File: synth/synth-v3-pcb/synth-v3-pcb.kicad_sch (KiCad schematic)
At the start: 34 parts, among them J1 Keyboard, J2 15mm Touch, J3 15mm Touch, U4 Pi Pico, U5 TC1044S

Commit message: Released Synth V3.0
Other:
- company: (none) -> LiveWires
- title: (none) -> LW Synth
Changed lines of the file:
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@@
 	(generator_version "9.0")
 	(paper "A4")
+	(title_block
+		(title "LW Synth")
+		(date "2026-01-06")
+		(rev "3.0")
+		(company "LiveWires")
+	)
 	(text "Power Regulator"
 		(exclude_from_sim no)
@@
 		)
 		(instances
-			(project "synth-v1"
+			(project "synth-v3-pcb"
 				(path "/e4b14e5f-7937-4e93-a8ca-bc52b5b8338f"
 					(page "2")

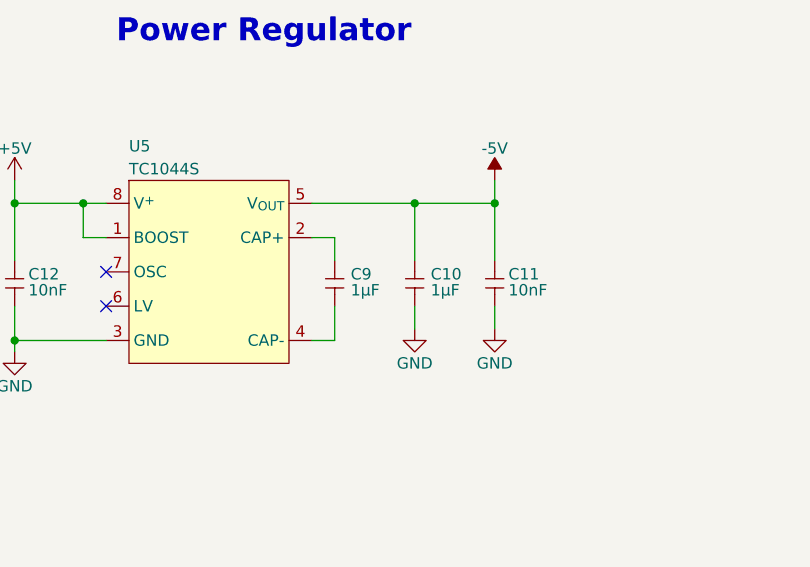
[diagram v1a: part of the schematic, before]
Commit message: Released PCB v3.1 and added knobs
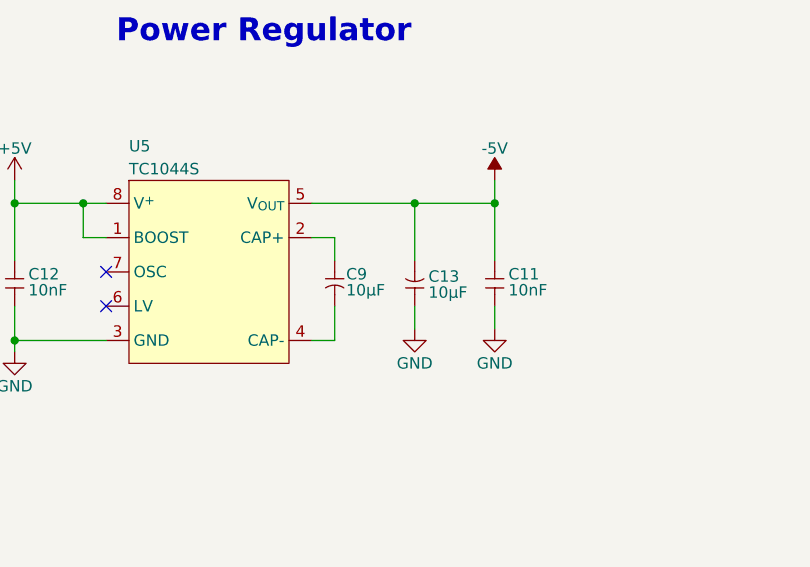
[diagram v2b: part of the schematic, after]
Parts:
- removed C10, C9: 1µF, LiveWires:LW_CeramicCap_5.08mm, symbol LiveWires:LW_C-1u
- added C13, C9: 10µF, LiveWires:LW_CAP_Radial_D5.0mm_P2.00mm, symbol LiveWires:LW_C-10u
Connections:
- net -5V: now also C13.2
- net GND: now also C13.1
- net at U5.2 (CAP+): now also C9.1
- net at U5.4 (CAP-): now also C9.2
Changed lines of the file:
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@@
-	)
-	(symbol
-		(lib_id "LiveWires:LW_C-1u")
-		(at 102.87 162.56 90)
-		(unit 1)
-		(exclude_from_sim no)
-		(in_bom yes)
-		(on_board yes)
-		(dnp no)
-		(property "Reference" "C10"
-			(at 104.648 161.544 90)
-			(effects
-				(font
-					(size 1.27 1.27)
-				)
-				(justify right)
-			)
-		)
-		(property "Value" "1µF"
-			(at 104.648 163.322 90)
-			(effects
-				(font
-					(size 1.27 1.27)
-				)
-				(justify right)
-			)
-		)
-		(property "Footprint" "LiveWires:LW_CeramicCap_5.08mm"
-			(at 102.87 162.56 0)
-			(effects
-				(font
-					(size 1.27 1.27)
-				)
-				(hide yes)
-			)
-		)
-		(property "Datasheet" ""
-			(at 102.87 162.56 0)
-			(effects
-				(font
-					(size 1.27 1.27)
-				)
-				(hide yes)
-			)
-		)
-		(property "Description" "1µF Ceramic Capacitor (generic)"
-			(at 102.87 162.56 0)
-			(effects
-				(font
-					(size 1.27 1.27)
-				)
-				(hide yes)
-			)
-		)
-		(property "Cost" "0.07"
-			(at 102.87 162.56 0)
-			(effects
-				(font
-					(size 1.27 1.27)
-				)
-				(hide yes)
-			)
-		)
-		(property "MPN" "TS170R1H105MSBFB0R"
-			(at 102.87 162.56 0)
-			(effects
-				(font
-					(size 1.27 1.27)
-				)
-				(hide yes)
-			)
-		)
-		(property "Manufacturer" "Suntan"
-			(at 102.87 162.56 0)
-			(effects
-				(font
-					(size 1.27 1.27)
-				)
-				(hide yes)
-			)
-		)
-		(pin "2"
-		)
-		(pin "1"
-		)
-		(instances
-			(project "synth-v1"
-				(path "/e4b14e5f-7937-4e93-a8ca-bc52b5b8338f"
-					(reference "C10")
-					(unit 1)
-				)
-			)
-		)
 	)
 	(symbol
@@
 	)
 	(symbol
+		(lib_id "LiveWires:LW_C-10u")
+		(at 102.87 162.56 270)
+		(unit 1)
+		(exclude_from_sim no)
+		(in_bom yes)
+		(on_board yes)
+		(dnp no)
+		(property "Reference" "C13"
+			(at 104.394 161.798 90)
+			(effects
+				(font
+					(size 1.27 1.27)
+				)
+				(justify left)
+			)
+		)
+		(property "Value" "10µF"
+			(at 104.394 163.576 90)
+			(effects
+				(font
+					(size 1.27 1.27)
+				)
+				(justify left)
+			)
+		)
+		(property "Footprint" "LiveWires:LW_CAP_Radial_D5.0mm_P2.00mm"
+			(at 102.87 162.56 0)
+			(effects
+				(font
+					(size 1.27 1.27)
+				)
+				(hide yes)
+			)
+		)
+		(property "Datasheet" ""
+			(at 102.87 162.56 0)
+			(effects
+				(font
+					(size 1.27 1.27)
+				)
+				(hide yes)
+			)
+		)
+		(property "Description" "10µF Electrolytic, Cap 5mm diameter, 2mm pitch, 25V"
+			(at 102.87 162.56 0)
+			(effects
+				(font
+					(size 1.27 1.27)
+				)
+				(hide yes)
+			)
+		)
+		(property "Cost" "0.014"
+			(at 102.87 162.56 0)
+			(effects
+				(font
+					(size 1.27 1.27)
+				)
+				(hide yes)
+			)
+		)
+		(property "MPN" "TS13DE1E100MSB030R"
+			(at 102.87 162.56 0)
+			(effects
+				(font
+					(size 1.27 1.27)
+				)
+				(hide yes)
+			)
+		)
+		(property "Manufacturer" "Suntan"
+			(at 102.87 162.56 0)
+			(effects
+				(font
+					(size 1.27 1.27)
+				)
+				(hide yes)
+			)
+		)
+		(pin "1"
+		)
+		(pin "2"
+		)
+		(instances
+			(project ""
+				(path "/e4b14e5f-7937-4e93-a8ca-bc52b5b8338f"
+					(reference "C13")
+					(unit 1)
+				)
+			)
+		)
+	)
+	(symbol
 		(lib_id "LiveWires:LW_R-100")
 		(at 260.35 50.8 0)
@@
 	)
 	(symbol
-		(lib_id "LiveWires:LW_C-1u")
+		(lib_id "LiveWires:LW_C-10u")
 		(at 93.98 162.56 90)
 		(unit 1)
@@
 		(dnp no)
 		(property "Reference" "C9"
-			(at 95.758 161.544 90)
+			(at 95.25 161.544 90)
 			(effects
 				(font
@@
 			)
 		)
-		(property "Value" "1µF"
-			(at 95.758 163.322 90)
+		(property "Value" "10µF"
+			(at 95.25 163.322 90)
 			(effects
 				(font
@@
 			)
 		)
-		(property "Footprint" "LiveWires:LW_CeramicCap_5.08mm"
+		(property "Footprint" "LiveWires:LW_CAP_Radial_D5.0mm_P2.00mm"
 			(at 93.98 162.56 0)
 			(effects
@@
 			)
 		)
-		(property "Description" "1µF Ceramic Capacitor (generic)"
+		(property "Description" "10µF Electrolytic, Cap 5mm diameter, 2mm pitch, 25V"
 			(at 93.98 162.56 0)
 			(effects
@@
 			)
 		)
-		(property "Cost" "0.07"
+		(property "Cost" "0.014"
 			(at 93.98 162.56 0)
 			(effects
@@
 			)
 		)
-		(property "MPN" "TS170R1H105MSBFB0R"
+		(property "MPN" "TS13DE1E100MSB030R"
 			(at 93.98 162.56 0)
 			(effects
@@
 			)
 		)
+		(pin "1"
+		)
 		(pin "2"
 		)
-		(pin "1"
-		)
 		(instances
-			(project "synth-v1"
+			(project "synth-v3-pcb"
 				(path "/e4b14e5f-7937-4e93-a8ca-bc52b5b8338f"
 					(reference "C9")
